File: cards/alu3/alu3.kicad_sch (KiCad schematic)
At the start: 126 parts, among them J1 BUS, J2 IN, Q1 2N7000, Q10 2N7000, Q11 2N7000, Q12 2N7000, Q13 2N7000, Q14 2N7000, Q15 2N7000, Q16 2N7000, Q17 2N7000, Q18 2N7000, Q19 2N7000, Q2 2N7000, Q20 2N7000, Q21 2N7000, Q22 2N7000, Q23 2N7000, Q24 2N7000, Q25 2N7000, Q26 2N7000, Q27 2N7000, Q28 2N7000, Q29 2N7000, Q3 2N7000, Q30 2N7000, Q31 2N7000, Q32 2N7000, Q33 2N7000, Q34 2N7000, Q35 2N7000, Q36 2N7000, Q37 2N7000, Q38 2N7000, Q39 2N7000, Q4 2N7000, Q40 2N7000, Q41 2N7000, Q42 2N7000, Q43 2N7000, Q44 2N7000, Q45 2N7000, Q46 2N7000, Q47 2N7000, Q48 2N7000, Q49 2N7000, Q5 2N7000, Q50 2N7000, Q51 2N7000, Q52 2N7000, Q53 2N7000, Q54 2N7000, Q55 2N7000, Q56 2N7000, Q57 2N7000, Q58 2N7000, Q59 2N7000, Q6 2N7000, Q60 2N7000, Q61 2N7000, Q62 2N7000, Q63 2N7000, Q64 2N7000, Q65 2N7000, Q66 2N7000, Q67 2N7000, Q68 2N7000, Q69 2N7000, Q7 2N7000, Q70 2N7000, Q71 2N7000, Q72 2N7000, Q73 2N7000, Q8 2N7000, Q9 2N7000

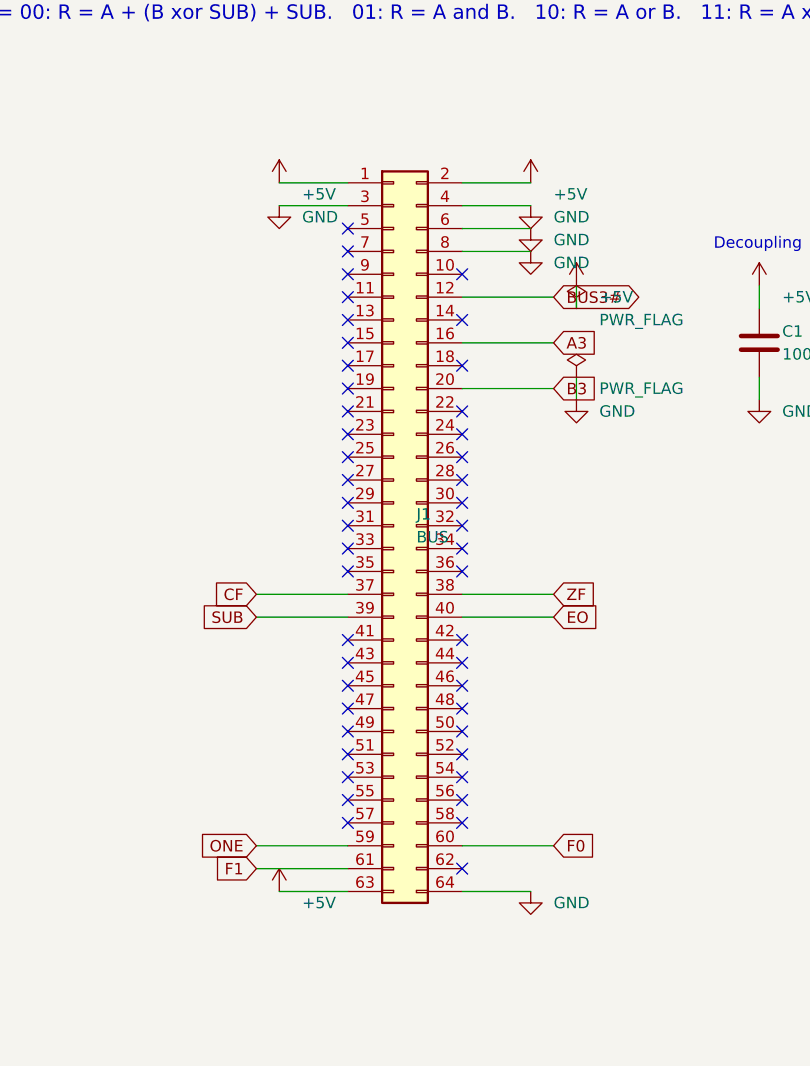
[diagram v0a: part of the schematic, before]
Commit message: The bus headers go on the back of all 26 boards, no track moved; the silkscreen refitted (D059, D062)
An IDC socket lies across its ribbon, so the ribbon could never run along a
row of cards as drawn. It runs behind them, and the 64-pin headers are
soldered on the back. This commit is that move, made in place on the routed
boards: no board was routed again.

How the header sits (D062): in the holes it had, turned over top to bottom,
notch toward the top edge. A pin of the odd row is then in the hole its even
neighbour had, so the two signals of every pair of pins change places: CLK
is pin 6, RST pin 8, +5V pins 1, 2 and 64. bus.py keeps both tables: PINS,
what the header's pins carry, and HOLES, what the copper was routed to.

The proof, on all 26 boards against 992a90f (sim/board_diff.py):
  netlist the same, element for element; every track, every via and every
  hole the same; each copper and mask layer differs by two pad shapes per
  header (pin 1's square went to the hole beside it, both on +5V) and the
  ground pour's outline round those two pads, nowhere else by more than a
  tenth of a micrometre.
sim/rebuild_check.py runs every builder into a scratch directory: each
writes the plan and the netlist that are committed, so a rebuild gives
this board. order_check.py --machine holds every pad of the 27 headers to
bus.py and requires them on the back.

What the move costs: on the ribbon RST had a ground conductor on both
sides; now one neighbour is BUS1#. tb_rst_neighbour.py puts the two lines
on the bench with every gate the routed boards hang on them: RST rises
0.28 to 0.43 V when BUS1# is released, against a lowest threshold of 0.8 V
(sim/results/rst_neighbour.md). The machine deck's crosstalk option now
couples the pins that are neighbours on the ribbon; the crosstalk stage of
the machine gate has to be run again on that order.

Silkscreen (pcb.fit_silk): every label to 1.0 mm where it has room, off
pads, vias, outlines and other labels, out from under the pa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
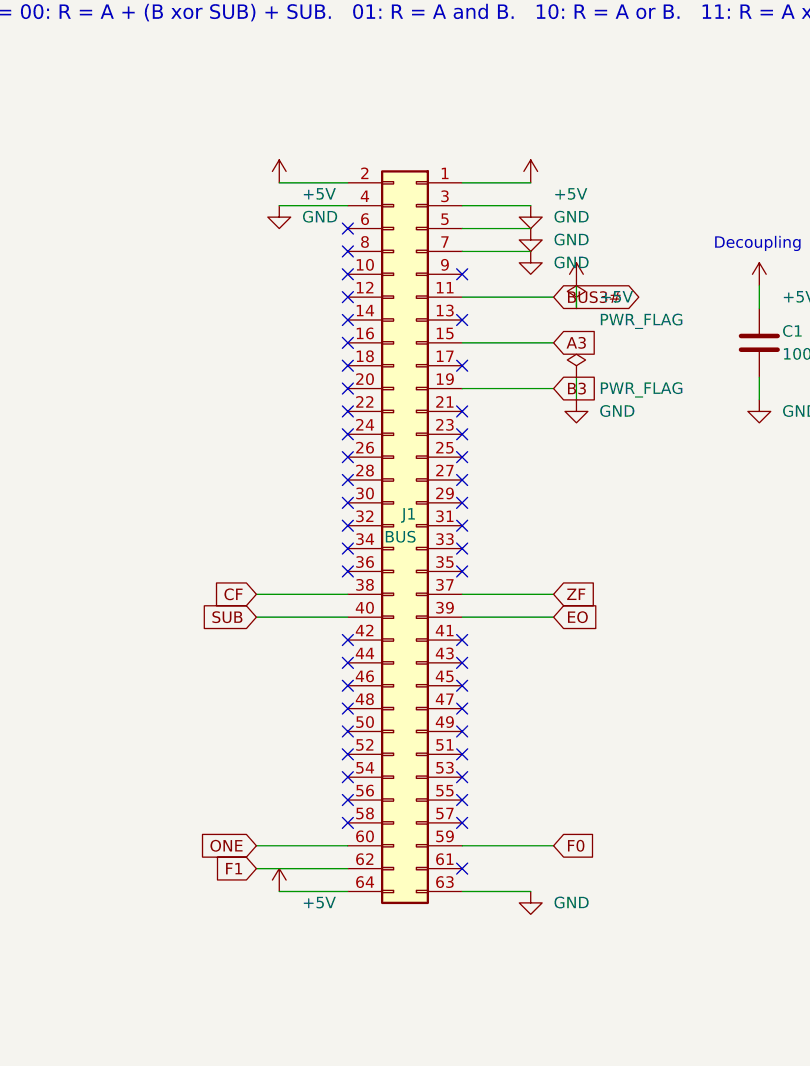
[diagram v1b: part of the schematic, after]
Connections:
- net +5V: now also J1.64 (Pin_64); no longer J1.63 (Pin_63)
- net A3: now also J1.15 (Pin_15); no longer J1.16 (Pin_16)
- net B3: now also J1.19 (Pin_19); no longer J1.20 (Pin_20)
- net BUS3#: now also J1.11 (Pin_11); no longer J1.12 (Pin_12)
- net CF: now also J1.38 (Pin_38); no longer J1.37 (Pin_37)
- net EO: now also J1.39 (Pin_39); no longer J1.40 (Pin_40)
- net F0: now also J1.59 (Pin_59); no longer J1.60 (Pin_60)
- net F1: now also J1.62 (Pin_62); no longer J1.61 (Pin_61)
- net GND: now also J1.5 (Pin_5), J1.63 (Pin_63), J1.7 (Pin_7); no longer J1.6 (Pin_6), J1.64 (Pin_64), J1.8 (Pin_8)
- net ONE: now also J1.60 (Pin_60); no longer J1.59 (Pin_59)
- net SUB: now also J1.40 (Pin_40); no longer J1.39 (Pin_39)
- net ZF: now also J1.37 (Pin_37); no longer J1.38 (Pin_38)
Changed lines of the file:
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@@
 	(symbol
 		(lib_id "Connector_Generic:Conn_02x32_Odd_Even")
-		(at 76.2 101.6 0)
+		(at 78.74 101.6 0)
+		(mirror y)
 		(unit 1)
 		(body_style 1)
